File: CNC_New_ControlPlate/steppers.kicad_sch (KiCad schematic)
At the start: 4 parts, among them U3 7406

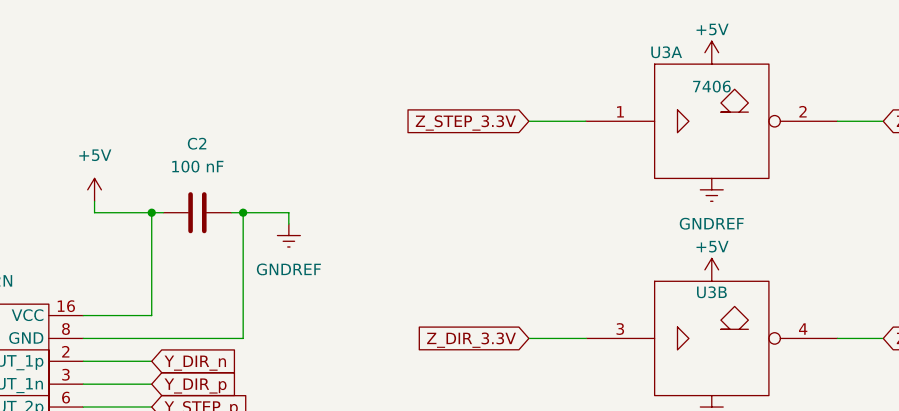
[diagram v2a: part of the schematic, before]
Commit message: Edit footprints
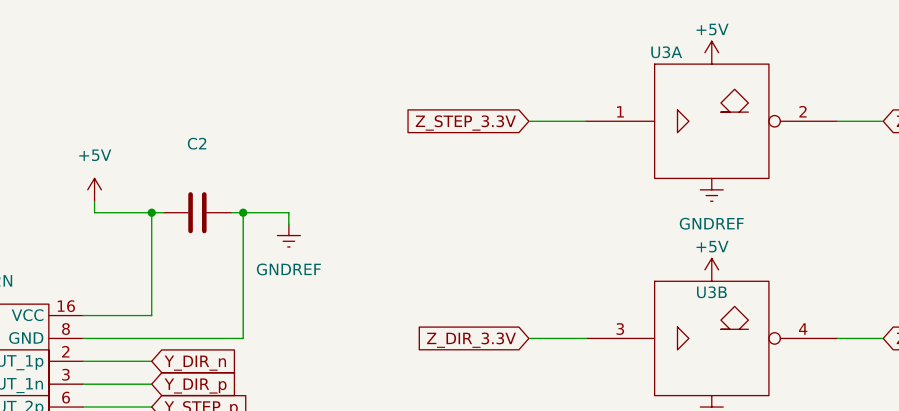
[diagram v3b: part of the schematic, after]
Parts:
- C2: value 100 nF -> (none); footprint Capacitor_SMD:C_0603_1608Metric_Pad1.08x0.95mm_HandSolder -> (none)
- U3: value 7406 -> (none); footprint Package_DIP:DIP-14_W7.62mm_Socket -> (none)
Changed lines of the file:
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@@
     (in_bom yes) (on_board yes)
     (property "Reference" "U3" (id 0) (at 147.32 50.8 0))
-    (property "Value" "7406" (id 1) (at 147.32 46.99 0)
-      (effects (font (size 1.27 1.27)) hide)
-    )
-    (property "Footprint" "Package_DIP:DIP-14_W7.62mm_Socket" (id 2) (at 147.32 55.88 0)
+    (property "Value" "" (id 1) (at 147.32 46.99 0)
+      (effects (font (size 1.27 1.27)) hide)
+    )
+    (property "Footprint" "" (id 2) (at 147.32 55.88 0)
       (effects (font (size 1.27 1.27)) hide)
     )
@@
     (in_bom yes) (on_board yes)
     (property "Reference" "U3" (id 0) (at 142.24 24.13 0))
-    (property "Value" "7406" (id 1) (at 147.32 27.94 0))
-    (property "Footprint" "Package_DIP:DIP-14_W7.62mm_Socket" (id 2) (at 147.32 31.75 0)
+    (property "Value" "" (id 1) (at 147.32 27.94 0))
+    (property "Footprint" "" (id 2) (at 147.32 31.75 0)
       (effects (font (size 1.27 1.27)) hide)
     )
@@
     (in_bom yes) (on_board yes) (fields_autoplaced)
     (property "Reference" "C2" (id 0) (at 90.17 34.29 90))
-    (property "Value" "100 nF" (id 1) (at 90.17 36.83 90))
-    (property "Footprint" "Capacitor_SMD:C_0603_1608Metric_Pad1.08x0.95mm_HandSolder" (id 2) (at 93.98 40.9448 0)
+    (property "Value" "" (id 1) (at 90.17 36.83 90))
+    (property "Footprint" "" (id 2) (at 93.98 40.9448 0)
       (effects (font (size 1.27 1.27)) hide)
     )
@@
     (in_bom yes) (on_board yes)
     (property "Reference" "U3" (id 0) (at 147.32 74.93 0))
-    (property "Value" "7406" (id 1) (at 147.32 71.12 0)
-      (effects (font (size 1.27 1.27)) hide)
-    )
-    (property "Footprint" "Package_DIP:DIP-14_W7.62mm_Socket" (id 2) (at 147.32 80.01 0)
-      (effects (font (size 1.27 1.27)) hide)
-    )
+    (property "Value" "" (id 1) (at 147.32 71.12 0)
+      (effects (font (size 1.27 1.27)) hide)
+    )
+    (property "Footprint" "" (id 2) (at 147.32 80.01 0)
+      (effects (font (size 1.27 1.27)) hide)
+    )

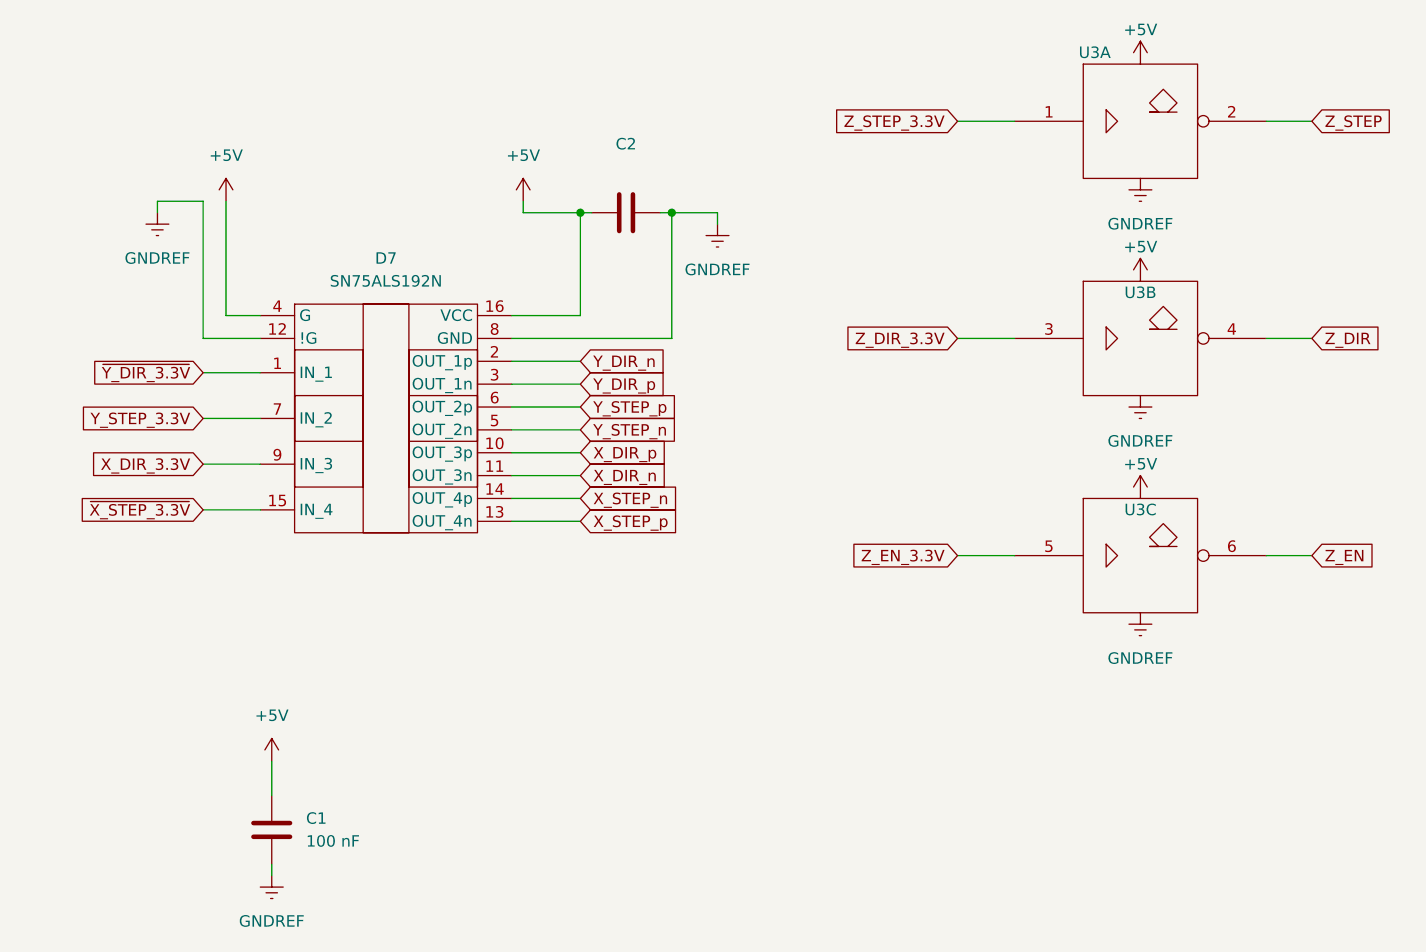
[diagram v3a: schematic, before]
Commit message: [*] Разводка платы в один слой (осталось 7 перемычек)
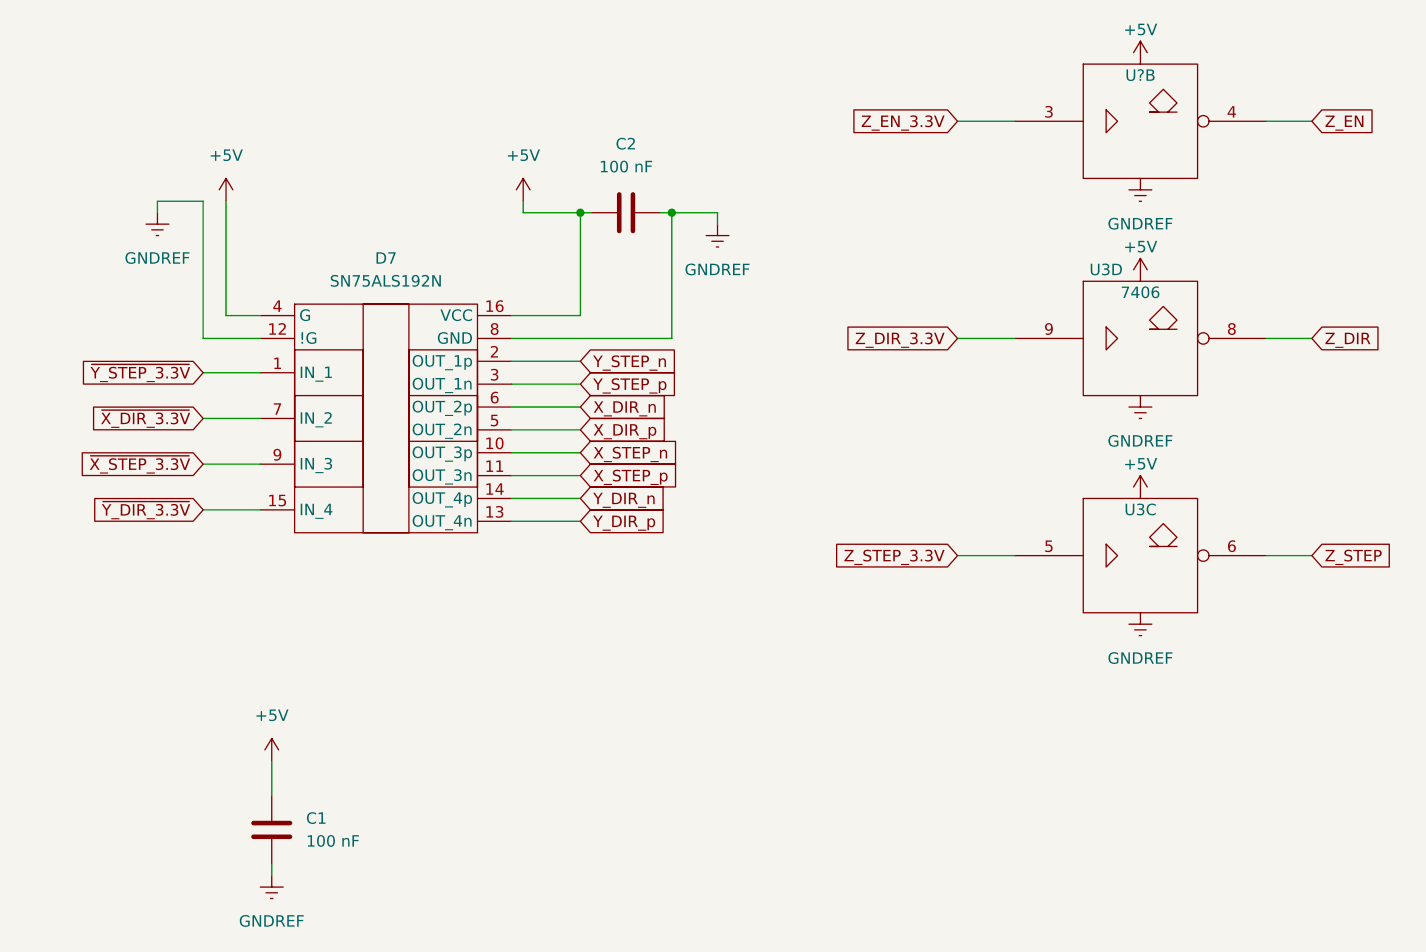
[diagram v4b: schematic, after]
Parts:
- removed unit 2 of U3
- removed unit 1 of U3
- added unit 4 of U3
- added U?: 7406, Package_DIP:DIP-14_W7.62mm_Socket, symbol 74xx_IEEE:7406
- C2: value (none) -> 100 nF; footprint (none) -> Capacitor_SMD:C_0603_1608Metric_Pad1.08x0.95mm_HandSolder
- U3: value (none) -> 7406; footprint (none) -> Package_DIP:DIP-14_W7.62mm_Socket
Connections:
- net X_DIR_3.3V is gone; now on net ~{X_STEP_3.3V}: D7.9 (IN_3)
- net +5V: now also U3.14 (Vcc), U?.14 (Vcc)
- net GNDREF: now also U3.7 (Gnd), U?.7 (Gnd)
- net X_DIR_n: now also D7.6 (OUT_2p); no longer D7.11 (OUT_3n)
- net X_DIR_p: now also D7.5 (OUT_2n); no longer D7.10 (OUT_3p)
- net X_STEP_n: now also D7.10 (OUT_3p); no longer D7.14 (OUT_4p)
- net X_STEP_p: now also D7.11 (OUT_3n); no longer D7.13 (OUT_4n)
- net Y_DIR_n: now also D7.14 (OUT_4p); no longer D7.2 (OUT_1p)
- net Y_DIR_p: now also D7.13 (OUT_4n); no longer D7.3 (OUT_1n)
- net Y_STEP_n: now also D7.2 (OUT_1p); no longer D7.5 (OUT_2n)
- net Y_STEP_p: now also D7.3 (OUT_1n); no longer D7.6 (OUT_2p)
- net Z_DIR: now also U3.8
- net Z_DIR_3.3V: now also U3.9
- net Z_EN: now also U?.4; no longer U3.6
- net Z_EN_3.3V: now also U?.3; no longer U3.5
- net Z_STEP: now also U3.6
- net Z_STEP_3.3V: now also U3.5
- net ~{X_STEP_3.3V}: no longer D7.15 (IN_4)
- net ~{Y_DIR_3.3V}: now also D7.15 (IN_4); no longer D7.1 (IN_1)
- net Y_STEP_3.3V renamed ~{X_DIR_3.3V}
- new net ~{Y_STEP_3.3V}: D7.1 (IN_1)

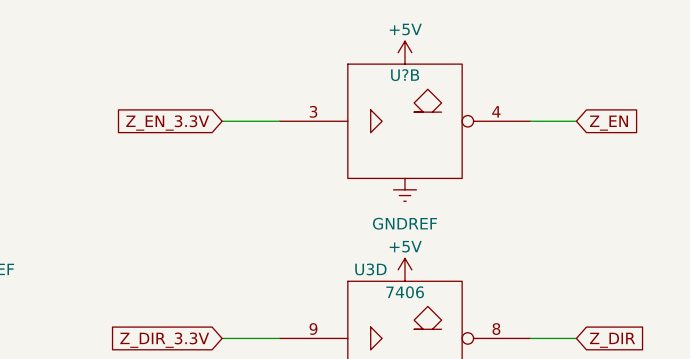
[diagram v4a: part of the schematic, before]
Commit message: [*] Разведена плата в один слой (3 перемычки на шине 5В; 2 соединения земли через плату STM
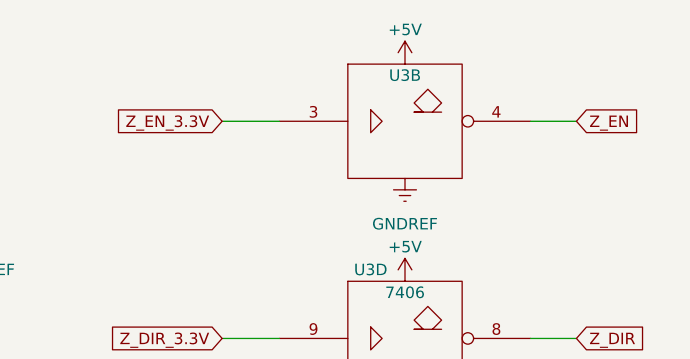
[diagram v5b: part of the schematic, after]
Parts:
- gave numbers to parts that had none: 1
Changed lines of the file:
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@@
   (symbol (lib_id "74xx_IEEE:7406") (at 147.32 31.75 0) (unit 2)
     (in_bom yes) (on_board yes)
-    (property "Reference" "U?" (id 0) (at 147.32 26.67 0))
+    (property "Reference" "U3" (id 0) (at 147.32 26.67 0))
     (property "Value" "7406" (id 1) (at 147.32 22.86 0)
       (effects (font (size 1.27 1.27)) hide)
